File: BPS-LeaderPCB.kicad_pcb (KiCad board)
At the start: 2 copper layers, 100 x 75 mm, 154 parts, among them J1 GPIO Analyzer, J10 CAN_Out, J11 ErrorLightConn, J12 USB_B_Micro, J13 FanBrdConn, J2 Volt/Temp SPI Analyzer, J3 Current SPI Analyzer, J4 CAN Analyzer, J5 SWD, J6 PowerConn, J7 MinionConn, J8 CurrentConn, J9 ContactorConn, Q1 NTR4003NT1G, Q2 VND5N07-E, Q3 NTR4003NT1G, Q4 VND5N07-E, SW1 B3SL-1002P, U1 STM32F413RHTx, U10 ADM3055E, U11 CDSOT23-T24CAN, U12 SI8261ABC-IS, U13 CP2102N-A01-GQFN24, U14 SI8261ABC-IS, U15 SI8261ABC-IS, U16 SI8261ABC-IS, U17 SI8261ABC-IS, U18 MCP112, U19 RN4871-I, U2 RI3-1205S, U3 NCP1117-3.3_SOT223, U4 M24128, U5 LTC6820, U6 LTC6820, U7 HX1188FNL, U8 SI8261ABC-IS, U9 BAS70-04, Y1 8M

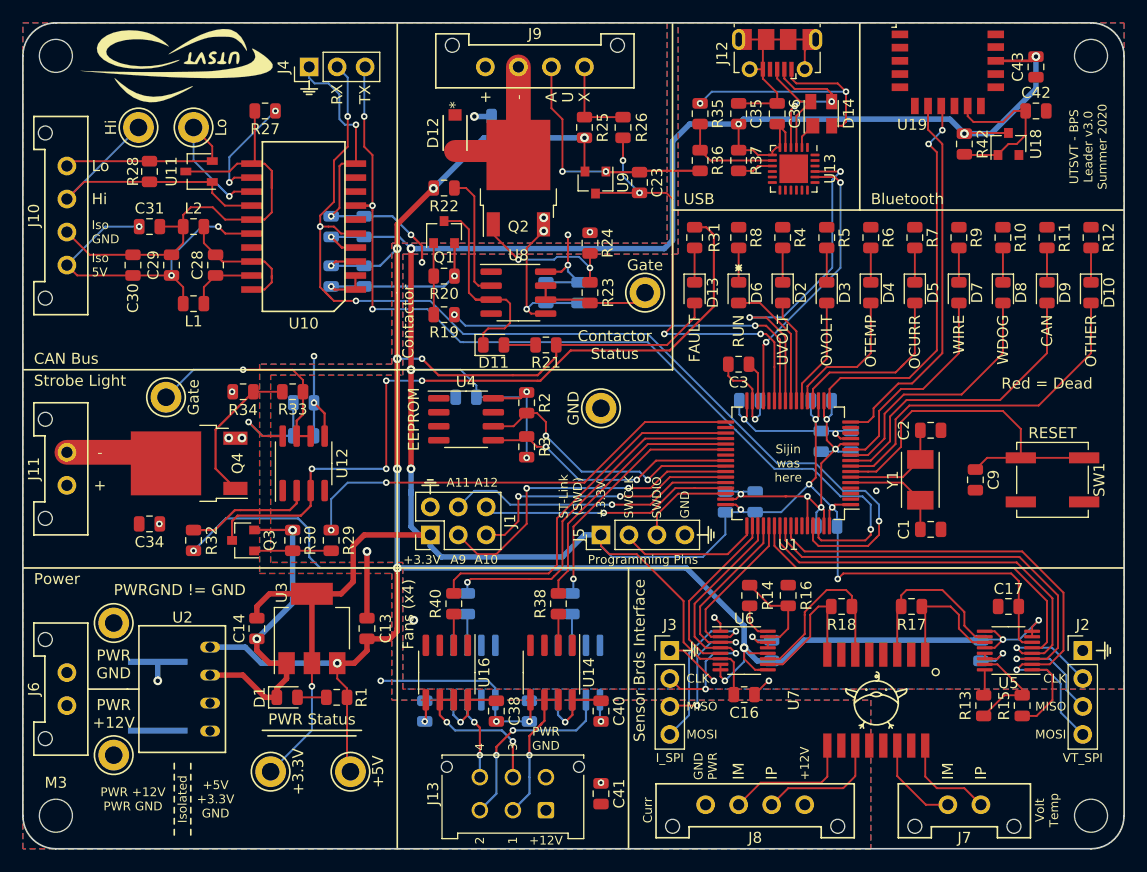
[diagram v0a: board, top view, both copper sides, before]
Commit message: Updates BAS70-04 footprint for Contactor auxillary interface
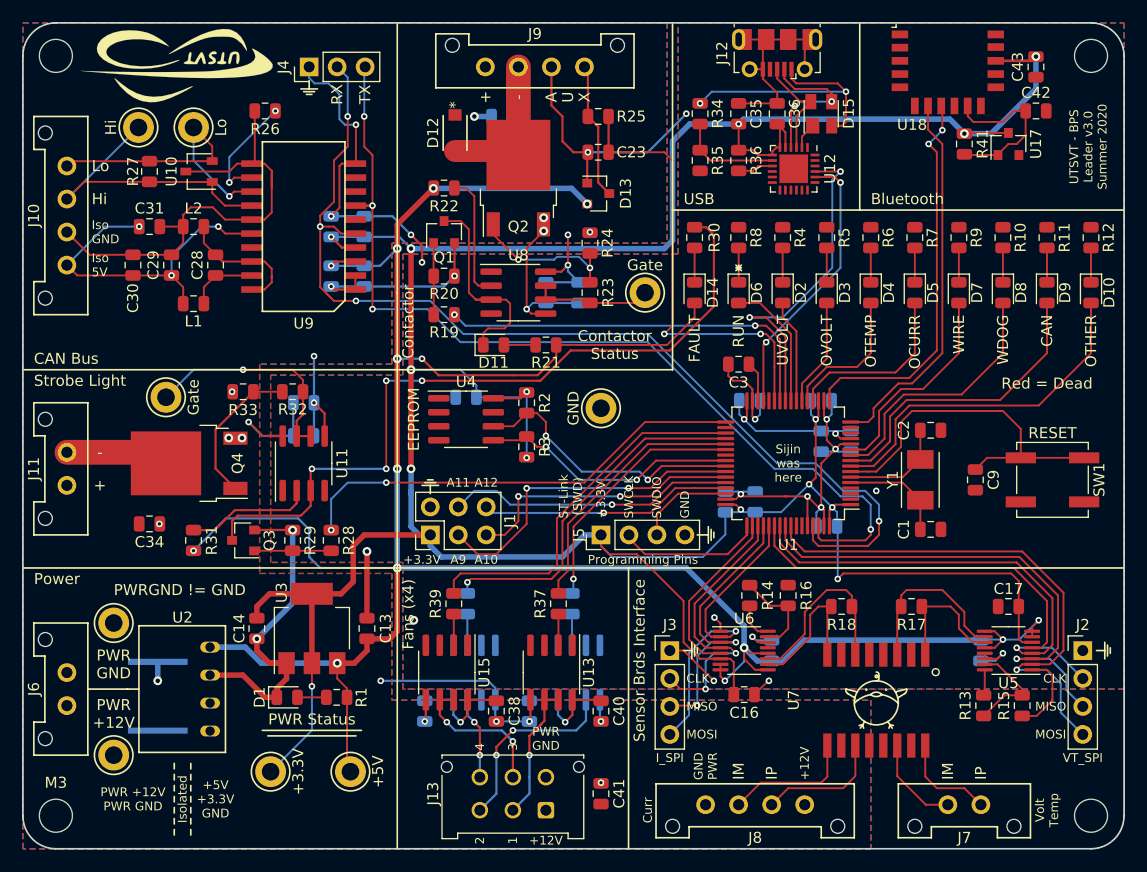
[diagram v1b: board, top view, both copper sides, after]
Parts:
- removed the R25 at (151.0, 59.5)
- removed the U9 at (152.0, 64.5)
- added D13: BAS70-04, Package_TO_SOT_SMD:SOT-23, F.Cu at (152.2, 65.5)
- moved C23 4.65 mm to (152.2, 61.8), turned to 180 degrees
- moved R25 2.46 mm to (152.2, 58.5), turned to 180 degrees
- renumbered D13 to D14, D14 to D15, R26 to R25, R27 to R26, R28 to R27, R29 to R28, R30 to R29, R31 to R30, R32 to R31, R33 to R32, R34 to R33, R35 to R34, R36 to R35, R37 to R36, R38 to R37, R39 to R38, R40 to R39, R41 to R40, R42 to R41, U11 to U10, U12 to U11, U13 to U12, U14 to U13, U15 to U14, U16 to U15, U17 to U16, U18 to U17, U19 to U18, U10 to U9
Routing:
- net Net-(D13-Pad3): track 8.06 -> 12.4 mm
- net +5V: track 236.2 -> 232.1 mm
- net GND: track 198.0 -> 198.6 mm
- net /PB1: vias 4 -> 2

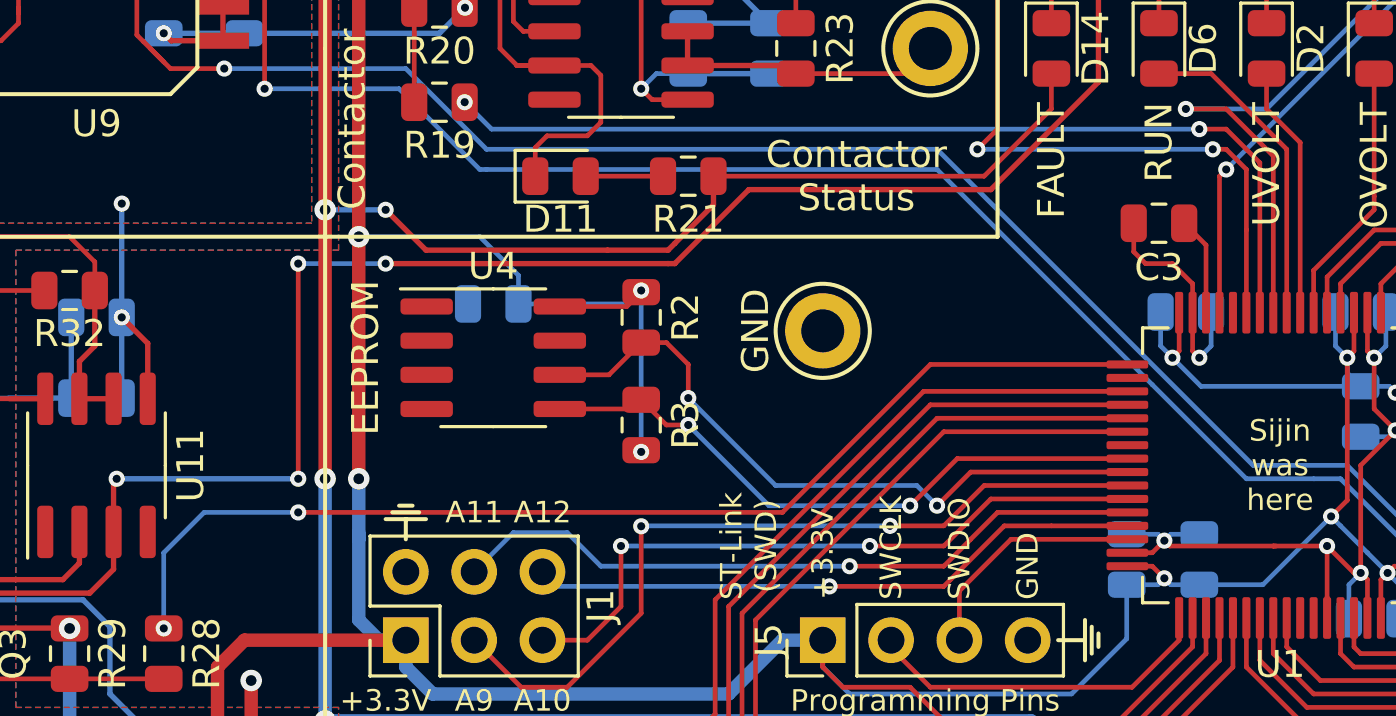
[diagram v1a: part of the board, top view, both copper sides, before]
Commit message: Changes clearance from 0.127 to .2mm:
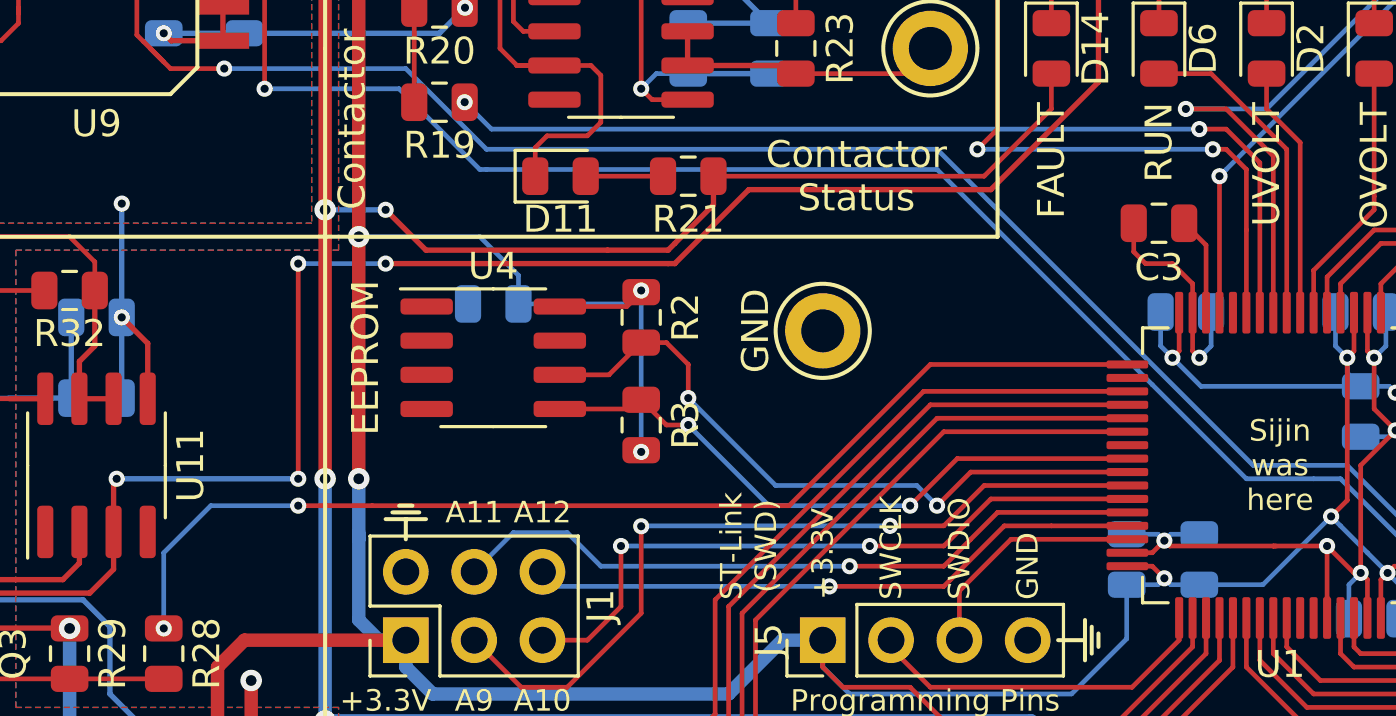
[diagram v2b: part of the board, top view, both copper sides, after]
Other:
- net class Default: clearance 0.127 -> 0.2
- rule trace_clearance: 0.127 -> 0.2
